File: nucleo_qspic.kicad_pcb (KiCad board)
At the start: 4 copper layers, 72.4 x 97.8 mm, 16 parts, among them IC1 W25Q32JVSFIQ, U1 NUCLEO144-H743ZI

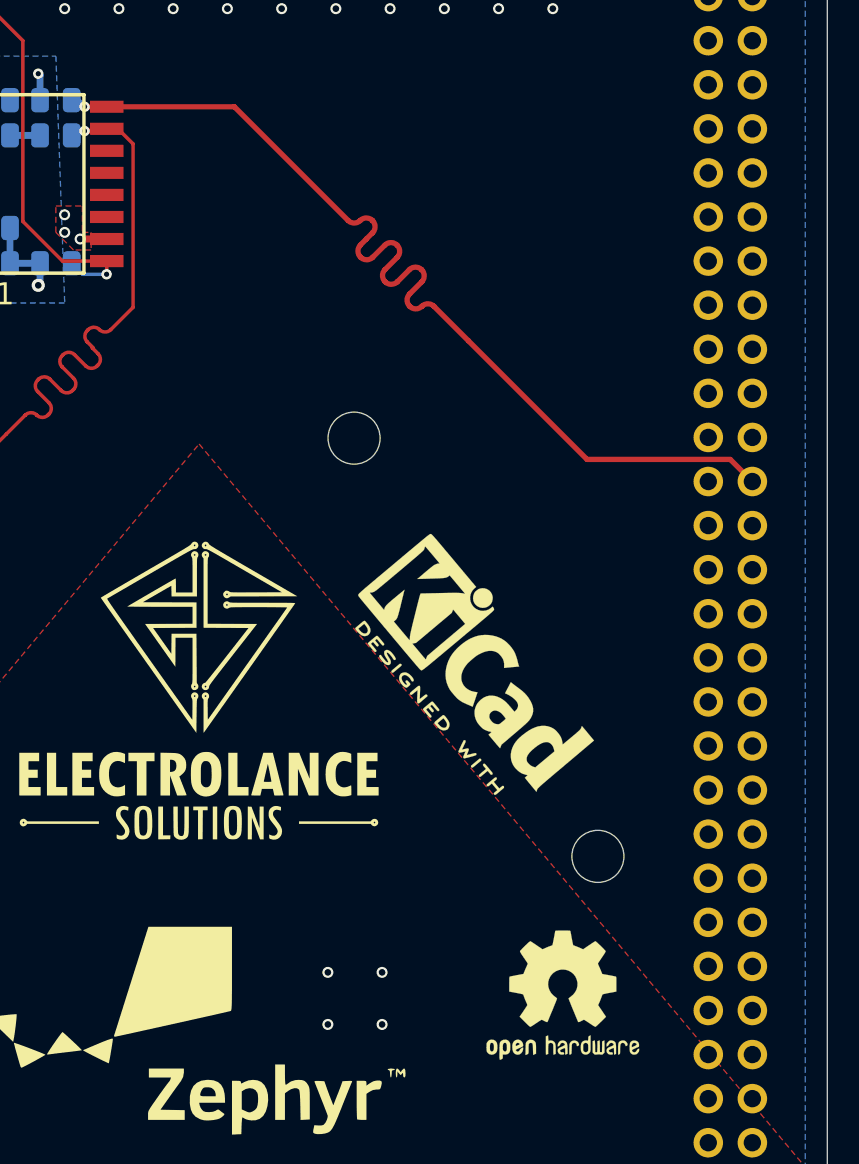
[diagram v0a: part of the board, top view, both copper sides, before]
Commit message: make clk line width same with other qspi signal, give pull up value to 10K(optional) and change capacitance value to what is available in inventory
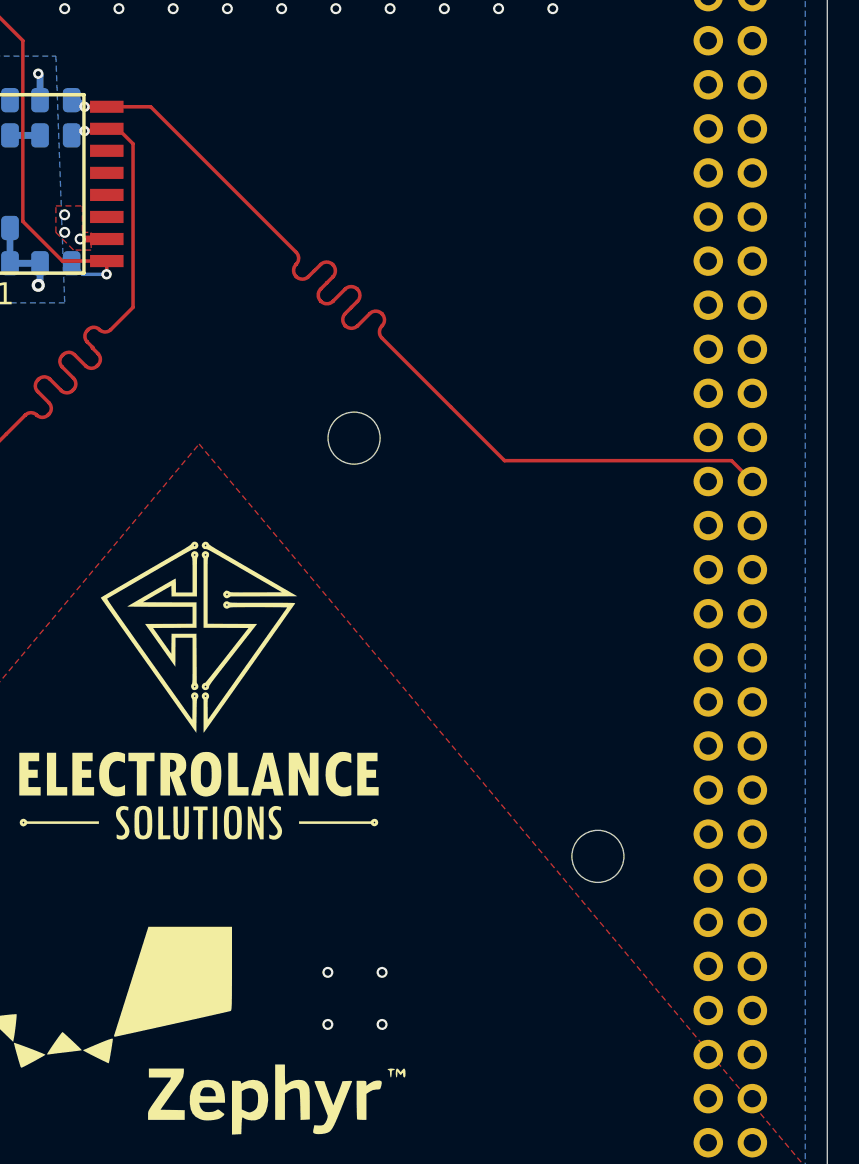
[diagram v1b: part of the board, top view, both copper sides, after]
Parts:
- removed REF**: KiCad-Logo2_6mm_SilkScreen, Symbol:KiCad-Logo2_6mm_SilkScreen
- removed REF**: OSHW-Logo2_9.8x8mm_SilkScreen, Symbol:OSHW-Logo2_9.8x8mm_SilkScreen
- C1: value 0.01uF -> 0.1uF
- C3: value 0.1uF -> DNP
- R1, R2, R3, R4, R5, R6, R7: value ? -> 10K
